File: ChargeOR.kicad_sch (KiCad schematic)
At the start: 5 parts, among them Q4 SiRA99DP, U4 LTC4412xS6

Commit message: v3.1 Updates
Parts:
- C34: renamed from C2; value 0.1uF -> 100n
- renumbered D7 to D6, F4 to F7, Q4 to Q9, U4 to U3
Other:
- company: (none) -> Carnegie Mellon University
- title: (none) -> Argus XY Solar Panel

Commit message: Local Stash
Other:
- moved on the sheet: C34, D6, F7, Q9, U3

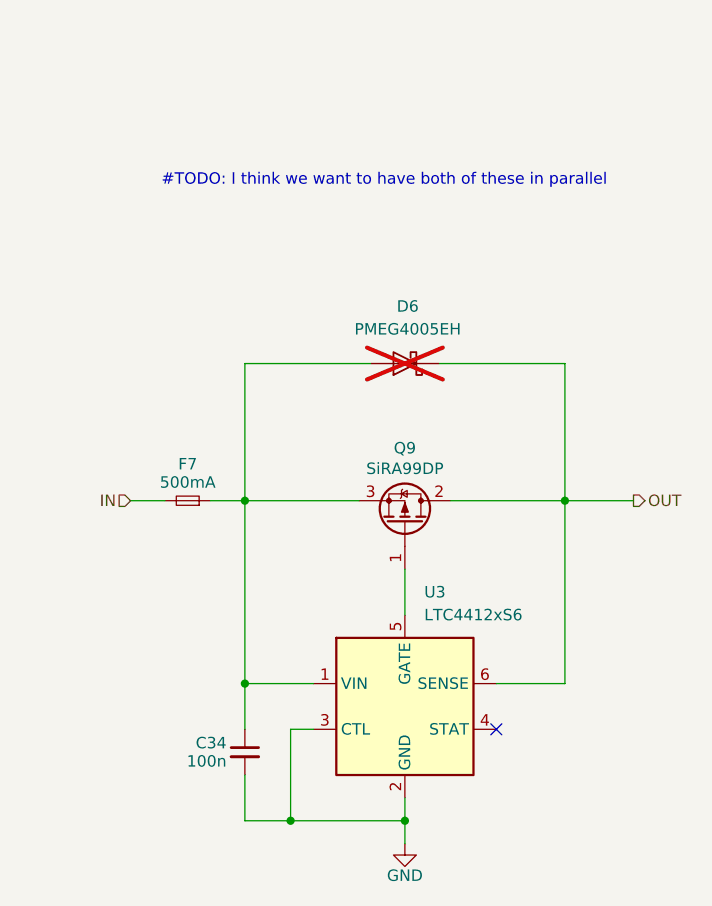
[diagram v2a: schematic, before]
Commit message: Updated access port, added deployment sensor
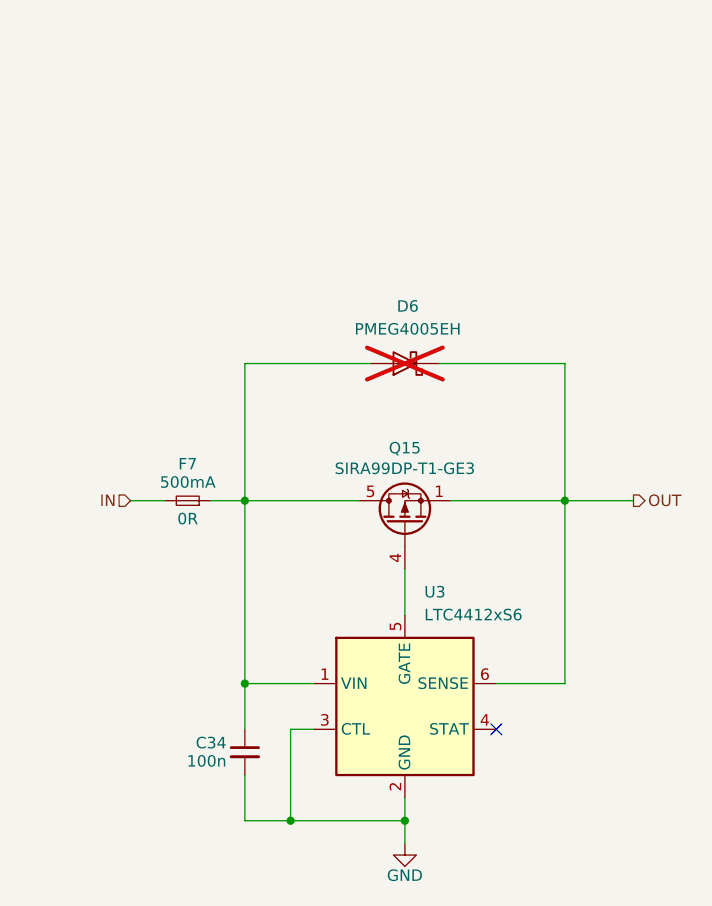
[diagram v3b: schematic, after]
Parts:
- removed Q9: SiRA99DP, Argus-Miscellaneous:PowerPAK SO-8, symbol Argus-IC:Q_PMOS_GDS
- added Q15: SIRA99DP-T1-GE3, Package_SO:PowerPAK_SO-8_Single, symbol Transistor_FET:Si7141DP
- C34: MPN (none) -> C307348
- D6: DNI (none) -> DNI; now left out of the parts list
- F7: Flight (none) -> 0R
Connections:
- net OUT: now also Q15.1 (S), Q15.2 (S), Q15.3 (S)
- net at C34.1, D6.2 (A), F7.1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: now also Q15.5 (D)
- net at U3.5 (GATE): now also Q15.4 (G)
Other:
- note removed: "#TODO: I think we want to have both of these in parallel"
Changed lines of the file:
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@@
 		(comment 2 "V. Rajesh")
-	)
-	(text "#TODO: I think we want to have both of these in parallel"
-		(exclude_from_sim no)
-		(at 145.034 58.42 0)
-		(effects
-			(font
-				(size 1.27 1.27)
-			)
-		)
 	)
 	(junction
@@
 			)
 			(justify left)
+		)
+	)
+	(symbol
+		(lib_id "Transistor_FET:Si7141DP")
+		(at 147.32 96.52 90)
+		(unit 1)
+		(exclude_from_sim no)
+		(in_bom yes)
+		(on_board yes)
+		(dnp no)
+		(property "Reference" "Q15"
+			(at 147.32 88.138 90)
+			(effects
+				(font
+					(size 1.27 1.27)
+				)
+			)
+		)
+		(property "Value" "SIRA99DP-T1-GE3"
+			(at 147.32 90.424 90)
+			(effects
+				(font
+					(size 1.27 1.27)
+				)
+			)
+		)
+		(property "Footprint" "Package_SO:PowerPAK_SO-8_Single"
+			(at 149.225 91.44 0)
+			(effects
+				(font
+					(size 1.27 1.27)
+					(italic yes)
+				)
+				(justify left)
+				(hide yes)
+			)
+		)
+		(property "Datasheet" "https://www.vishay.com/docs/65596/si7141dp.pdf"
+			(at 151.13 91.44 0)
+			(effects
+				(font
+					(size 1.27 1.27)
+				)
+				(justify left)
+				(hide yes)
+			)
+		)
+		(property "Description" "-60A Id, -20V Vds, 1.9 mOhm Ron, PowerPAK-8"
+			(at 147.32 96.52 0)
+			(effects
+				(font
+					(size 1.27 1.27)
+				)
+				(hide yes)
+			)
+		)
+		(property "MPN" "C3289459"
+			(at 147.32 96.52 90)
+			(effects
+				(font
+					(size 1.27 1.27)
+				)
+				(hide yes)
+			)
+		)
+		(pin "5"
+		)
+		(pin "2"
+		)
+		(pin "3"
+		)
+		(pin "4"
+		)
+		(pin "1"
+		)
+		(instances
+			(project "Avionics-SolarPanels"
+				(path "/92e58b76-9357-4452-b231-18fffdf58e73/bef00a2e-eb3a-4ecf-812a-1c3ccf6e8d66/16f90485-8271-472f-a87a-9c27ffab6e8f"
+					(reference "Q16")
+					(unit 1)
+				)
+				(path "/92e58b76-9357-4452-b231-18fffdf58e73/bef00a2e-eb3a-4ecf-812a-1c3ccf6e8d66/6c74510c-fc2f-4690-9a5b-9f1baf296eee"
+					(reference "Q15")
+					(unit 1)
+				)
+				(path "/92e58b76-9357-4452-b231-18fffdf58e73/bef00a2e-eb3a-4ecf-812a-1c3ccf6e8d66/b4f3b5ea-3783-47e9-83c1-86877692286f"
+					(reference "Q17")
+					(unit 1)
+				)
+			)
 		)
 	)
@@
 			)
 		)
+		(property "MPN" "C307348"
+			(at 129.54 121.92 0)
+			(effects
+				(font
+					(size 1.27 1.27)
+				)
+				(hide yes)
+			)
+		)
 		(pin "2"
 		)
@@
 			)
 		)
+		(property "Flight" "0R"
+			(at 123.19 96.012 0)
+			(effects
+				(font
+					(size 1.27 1.27)
+				)
+			)
+		)
 		(pin "2"
 		)
@@
 				(path "/92e58b76-9357-4452-b231-18fffdf58e73/bef00a2e-eb3a-4ecf-812a-1c3ccf6e8d66/b4f3b5ea-3783-47e9-83c1-86877692286f"
 					(reference "F9")
-					(unit 1)
-				)
-			)
-		)
-	)
-	(symbol
-		(lib_id "Argus-IC:Q_PMOS_GDS")
-		(at 147.32 96.52 270)
-		(mirror x)
-		(unit 1)
-		(exclude_from_sim no)
-		(in_bom yes)
-		(on_board yes)
-		(dnp no)
-		(property "Reference" "Q9"
-			(at 147.32 88.138 90)
-			(effects
-				(font
-					(size 1.27 1.27)
-				)
-			)
-		)
-		(property "Value" "SiRA99DP"
-			(at 147.32 90.424 90)
-			(effects
-				(font
-					(size 1.27 1.27)
-				)
-			)
-		)
-		(property "Footprint" "Argus-Miscellaneous:PowerPAK SO-8"
-			(at 149.86 91.44 0)
-			(effects
-				(font
-					(size 1.27 1.27)
-				)
-				(hide yes)
-			)
-		)
-		(property "Datasheet" "~"
-			(at 147.32 96.52 0)
-			(effects
-				(font
-					(size 1.27 1.27)
-				)
-				(hide yes)
-			)
-		)
-		(property "Description" "P-MOSFET transistor, gate/drain/source"
-			(at 147.32 96.52 0)
-			(effects
-				(font
-					(size 1.27 1.27)
-				)
-				(hide yes)
-			)
-		)
-		(pin "3"
-		)
-		(pin "2"
-		)
-		(pin "1"
-		)
-		(instances
-			(project ""
-				(path "/92e58b76-9357-4452-b231-18fffdf58e73/bef00a2e-eb3a-4ecf-812a-1c3ccf6e8d66/16f90485-8271-472f-a87a-9c27ffab6e8f"
-					(reference "Q10")
-					(unit 1)
-				)
-				(path "/92e58b76-9357-4452-b231-18fffdf58e73/bef00a2e-eb3a-4ecf-812a-1c3ccf6e8d66/6c74510c-fc2f-4690-9a5b-9f1baf296eee"
-					(reference "Q9")
-					(unit 1)
-				)
-				(path "/92e58b76-9357-4452-b231-18fffdf58e73/bef00a2e-eb3a-4ecf-812a-1c3ccf6e8d66/b4f3b5ea-3783-47e9-83c1-86877692286f"
-					(reference "Q11")
 					(unit 1)
 				)
@@
 		(unit 1)
 		(exclude_from_sim no)
-		(in_bom yes)
+		(in_bom no)
 		(on_board yes)
 		(dnp yes)
@@
 			(at 147.32 78.74 0)
 			(effects
+				(font
+					(size 1.27 1.27)
+				)
+				(hide yes)
+			)
+		)
+		(property "DNI" "DNI"
+			(at 147.32 78.74 0)
+			(effects
